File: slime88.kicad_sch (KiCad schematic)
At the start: 35 parts, among them J1 USB_C, J2 SWD, J3 JST-SH-4P, J4 Pin Breakout, SW0 Boot, U1 XC6206, U2 RP2040, U3 SRV05-4, U4 W25Q128JVS, Y1 12MHz

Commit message: Updated BOM inclusions
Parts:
- J4: now left out of the parts list
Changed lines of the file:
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@@
   )
   (symbol (lib_id "Connector_Generic:Conn_01x08") (at 125.73 227.33 0) (unit 1)
-    (in_bom yes) (on_board yes)
+    (in_bom no) (on_board yes)
     (property "Reference" "J4" (id 0) (at 128.27 227.33 0)
       (effects (font (size 1.27 1.27)) (justify left))

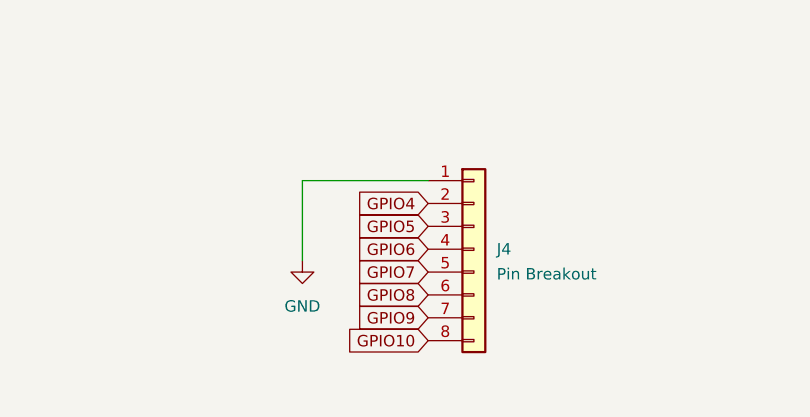
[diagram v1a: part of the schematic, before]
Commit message: Broke out 3v3 and 5v on Pin Breakout
Suggested by https://github.com/vinorodrigues

Slightly changed silkscreen (SWD -> SWDIO, Added boot indicator on the top silk)

Rewired some of the matrix to appropriately fit the 3v3 and 5v traces.
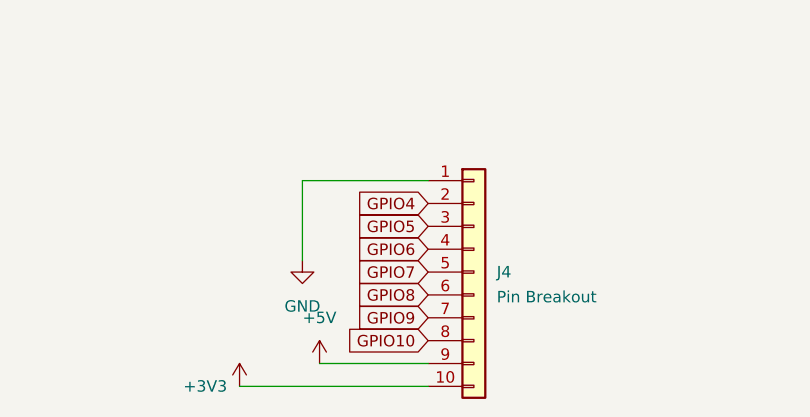
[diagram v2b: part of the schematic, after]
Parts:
- J4: footprint Connector_PinSocket_2.54mm:PinSocket_1x08_P2.54mm_Vertical -> Connector_PinSocket_2.54mm:PinSocket_1x10_P2.54mm_Vertical; symbol Connector_Generic:Conn_01x08 -> Connector_Generic:Conn_01x10
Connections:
- net +3V3: now also J4.10 (Pin_10)
- net +5V: now also J4.9 (Pin_9)
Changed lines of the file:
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@@
+    (stroke (width 0) (type default) (color 0 0 0 0))
+  )
+  (wire (pts (xy 108.585 240.03) (xy 120.65 240.03))
     (stroke (width 0) (type default) (color 0 0 0 0))
   )
@@
   )
   (wire (pts (xy 45.72 97.79) (xy 27.94 97.79))
+    (stroke (width 0) (type default) (color 0 0 0 0))
+  )
+  (wire (pts (xy 99.695 242.57) (xy 120.65 242.57))
     (stroke (width 0) (type default) (color 0 0 0 0))
   )
@@
     (pin "1")
     (pin "2")
+  )
+  (symbol (lib_id "power:+3V3") (at 99.695 242.57 0) (unit 1)
+    (in_bom yes) (on_board yes)
+    (property "Reference" "#PWR0106" (id 0) (at 99.695 246.38 0)
+      (effects (font (size 1.27 1.27)) hide)
+    )
+    (property "Value" "+3V3" (id 1) (at 95.885 242.57 0))
+    (property "Footprint" "" (id 2) (at 99.695 242.57 0)
+      (effects (font (size 1.27 1.27)) hide)
+    )
+    (property "Datasheet" "" (id 3) (at 99.695 242.57 0)
+      (effects (font (size 1.27 1.27)) hide)
+    )
+    (pin "1")
   )
   (symbol (lib_id "Connector_Generic:Conn_01x05") (at 234.95 116.84 0) (mirror y) (unit 1)
@@
     (pin "1")
   )
-  (symbol (lib_id "Connector_Generic:Conn_01x08") (at 125.73 227.33 0) (unit 1)
+  (symbol (lib_id "Connector_Generic:Conn_01x10") (at 125.73 229.87 0) (unit 1)
     (in_bom no) (on_board yes)
-    (property "Reference" "J4" (id 0) (at 128.27 227.33 0)
-      (effects (font (size 1.27 1.27)) (justify left))
-    )
-    (property "Value" "Pin Breakout" (id 1) (at 128.27 230.1051 0)
-      (effects (font (size 1.27 1.27)) (justify left))
-    )
-    (property "Footprint" "Connector_PinSocket_2.54mm:PinSocket_1x08_P2.54mm_Vertical" (id 2) (at 125.73 227.33 0)
-      (effects (font (size 1.27 1.27)) hide)
-    )
-    (property "Datasheet" "~" (id 3) (at 125.73 227.33 0)
-      (effects (font (size 1.27 1.27)) hide)
-    )
-    (pin "1")
+    (property "Reference" "J4" (id 0) (at 128.27 229.87 0)
+      (effects (font (size 1.27 1.27)) (justify left))
+    )
+    (property "Value" "Pin Breakout" (id 1) (at 128.27 232.6451 0)
+      (effects (font (size 1.27 1.27)) (justify left))
+    )
+    (property "Footprint" "Connector_PinSocket_2.54mm:PinSocket_1x10_P2.54mm_Vertical" (id 2) (at 125.73 229.87 0)
+      (effects (font (size 1.27 1.27)) hide)
+    )
+    (property "Datasheet" "~" (id 3) (at 125.73 229.87 0)
+      (effects (font (size 1.27 1.27)) hide)
+    )
+    (pin "1")
+    (pin "10")
     (pin "2")
     (pin "3")
@@
     (pin "7")
     (pin "8")
+    (pin "9")
   )
   (symbol (lib_id "Device:Crystal_GND24_Small") (at 182.88 115.57 90) (unit 1)
@@
     (pin "2")
   )
+  (symbol (lib_id "power:+5V") (at 108.585 240.03 0) (unit 1)
+    (in_bom yes) (on_board yes) (fields_autoplaced)
+    (property "Reference" "#PWR0105" (id 0) (at 108.585 243.84 0)
+      (effects (font (size 1.27 1.27)) hide)
+    )
+    (property "Value" "+5V" (id 1) (at 108.585 234.95 0))
+    (property "Footprint" "" (id 2) (at 108.585 240.03 0)
+      (effects (font (size 1.27 1.27)) hide)
+    )
+    (property "Datasheet" "" (id 3) (at 108.585 240.03 0)
+      (effects (font (size 1.27 1.27)) hide)
+    )
+    (pin "1")
+  )
   (symbol (lib_id "Device:C_Small") (at 272.415 72.39 0) (unit 1)
     (in_bom yes) (on_board yes)
@@
       (reference "#PWR0104") (unit 1) (value "GND") (footprint "")
     )
+    (path "/ec6af255-3fed-4d18-a575-0bef521de184"
+      (reference "#PWR0105") (unit 1) (value "+5V") (footprint "")
+    )
+    (path "/44a26aca-4ebd-4927-878e-ba6db571d1b9"
+      (reference "#PWR0106") (unit 1) (value "+3V3") (footprint "")
+    )
     (path "/29f11a32-f398-46d6-95a0-57f3be58392e"
       (reference "C1") (unit 1) (value "1uF") (footprint "Capacitor_SMD:C_0402_1005Metric")
@@
     )
     (path "/7e5da8d0-bec9-4daa-a9a1-871fdaa0d15e"
-      (reference "J4") (unit 1) (value "Pin Breakout") (footprint "Connector_PinSocket_2.54mm:PinSocket_1x08_P2.54mm_Vertical")
+      (reference "J4") (unit 1) (value "Pin Breakout") (footprint "Connector_PinSocket_2.54mm:PinSocket_1x10_P2.54mm_Vertical")
     )
     (path "/d5f64c48-5769-4554-8a1d-d23f7b2152b1"

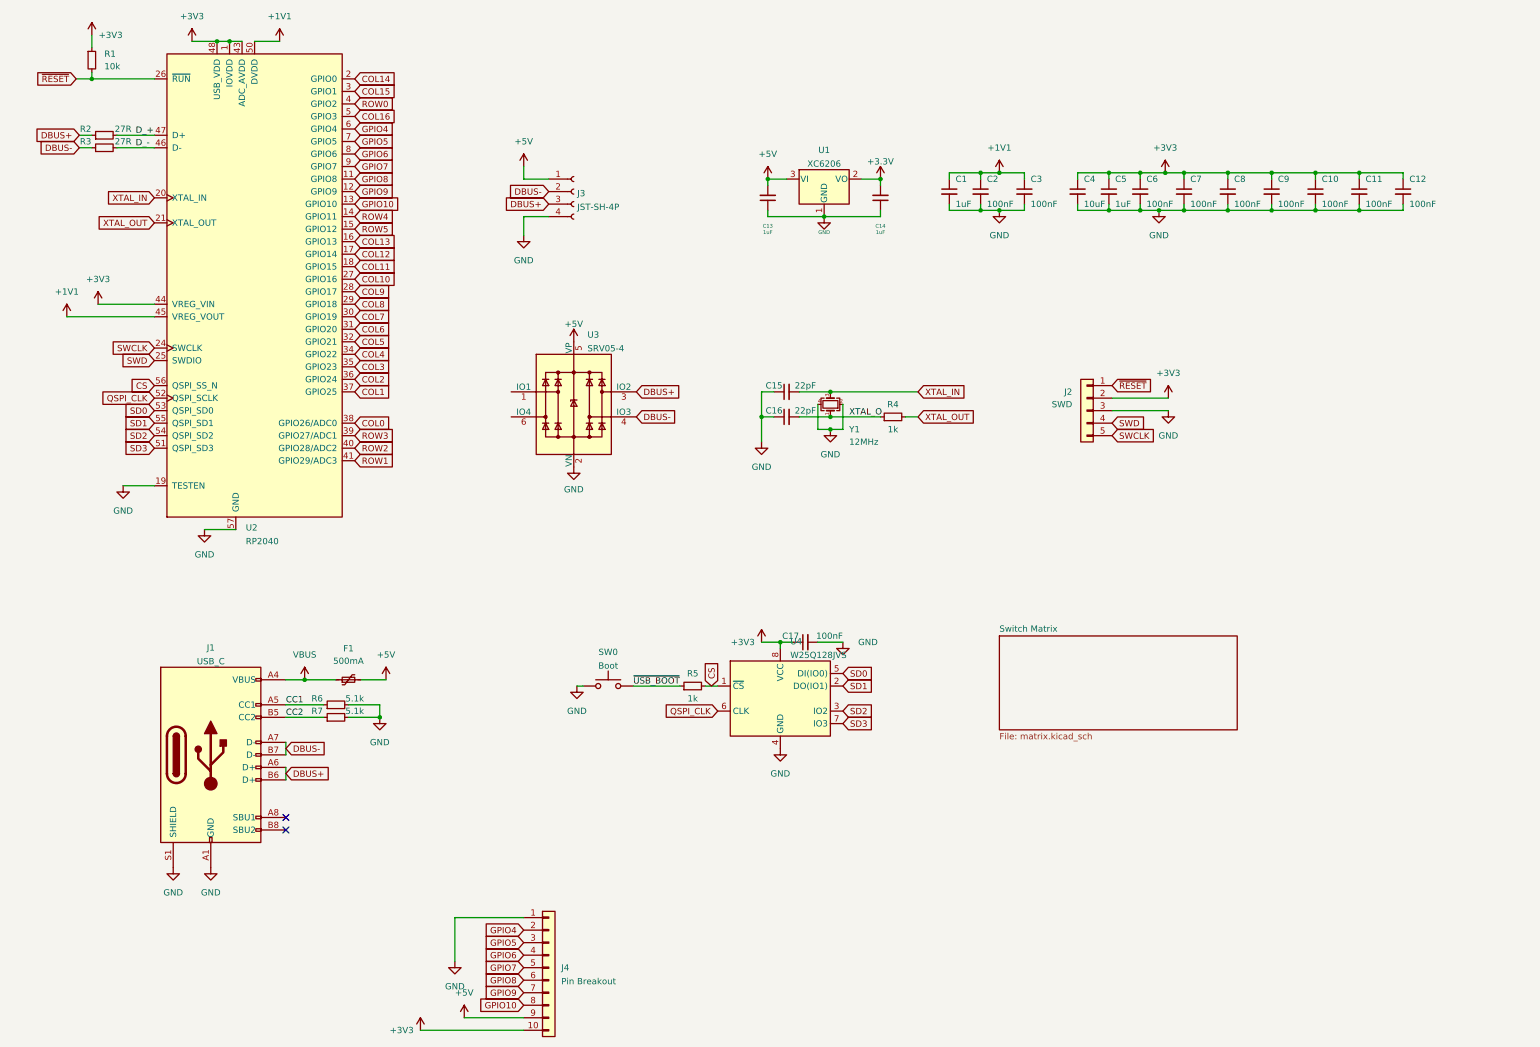
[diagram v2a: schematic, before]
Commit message: Generated manufacturing files (JLC), Updated Sleep-lib to a submodule, updated manufacturing files/part numbers
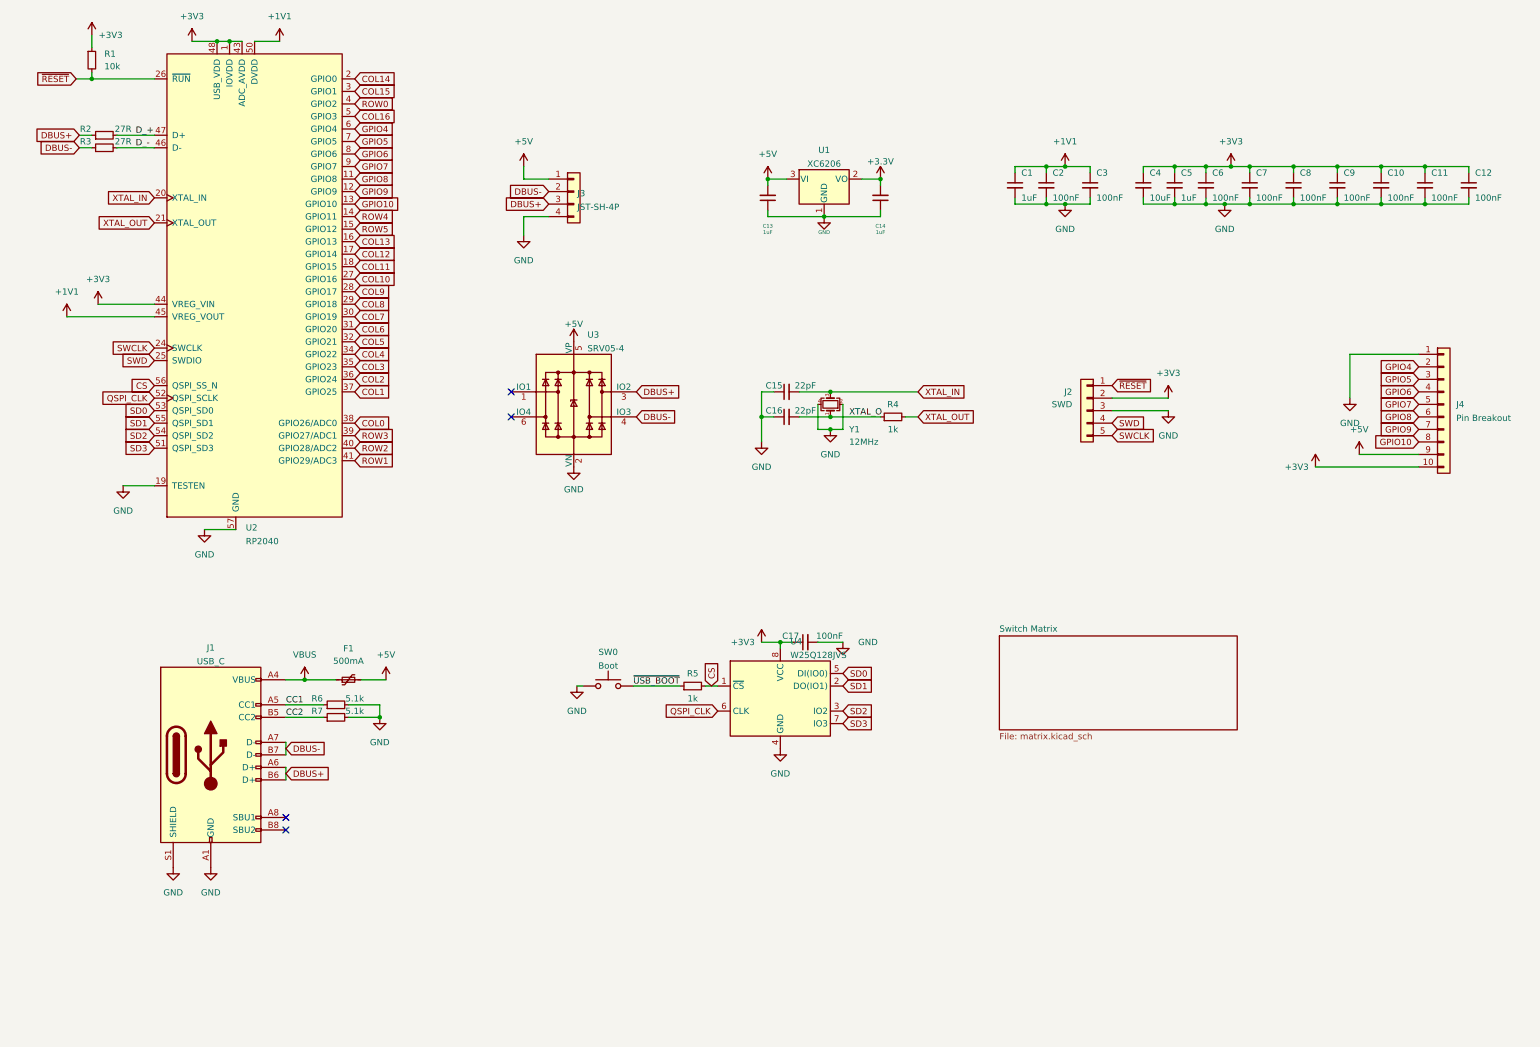
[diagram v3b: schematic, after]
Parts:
- J1: LCSC (none) -> C165948
- J3: symbol Connector:Conn_01x04_Female -> Connector_Generic:Conn_01x04; LCSC (none) -> C145956
- SW0: LCSC (none) -> C5156480
- U1: LCSC (none) -> C5446
- U2: LCSC (none) -> C2040
- U3: LCSC (none) -> C85364
- U4: LCSC (none) -> C97521
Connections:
- no-connect marks 2 -> 4
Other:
- moved on the sheet: C1, C10, C11, C12, C2, C3, C4, C5, C6, C7, C8, C9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
